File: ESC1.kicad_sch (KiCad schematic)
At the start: 35 parts, among them J7 SWD1, J8 MOTOR1, Q1 XRS306D, Q2 XRS306D, Q3 XRS306D, U8 STM32G071GBUxN, U9 DRV8300D

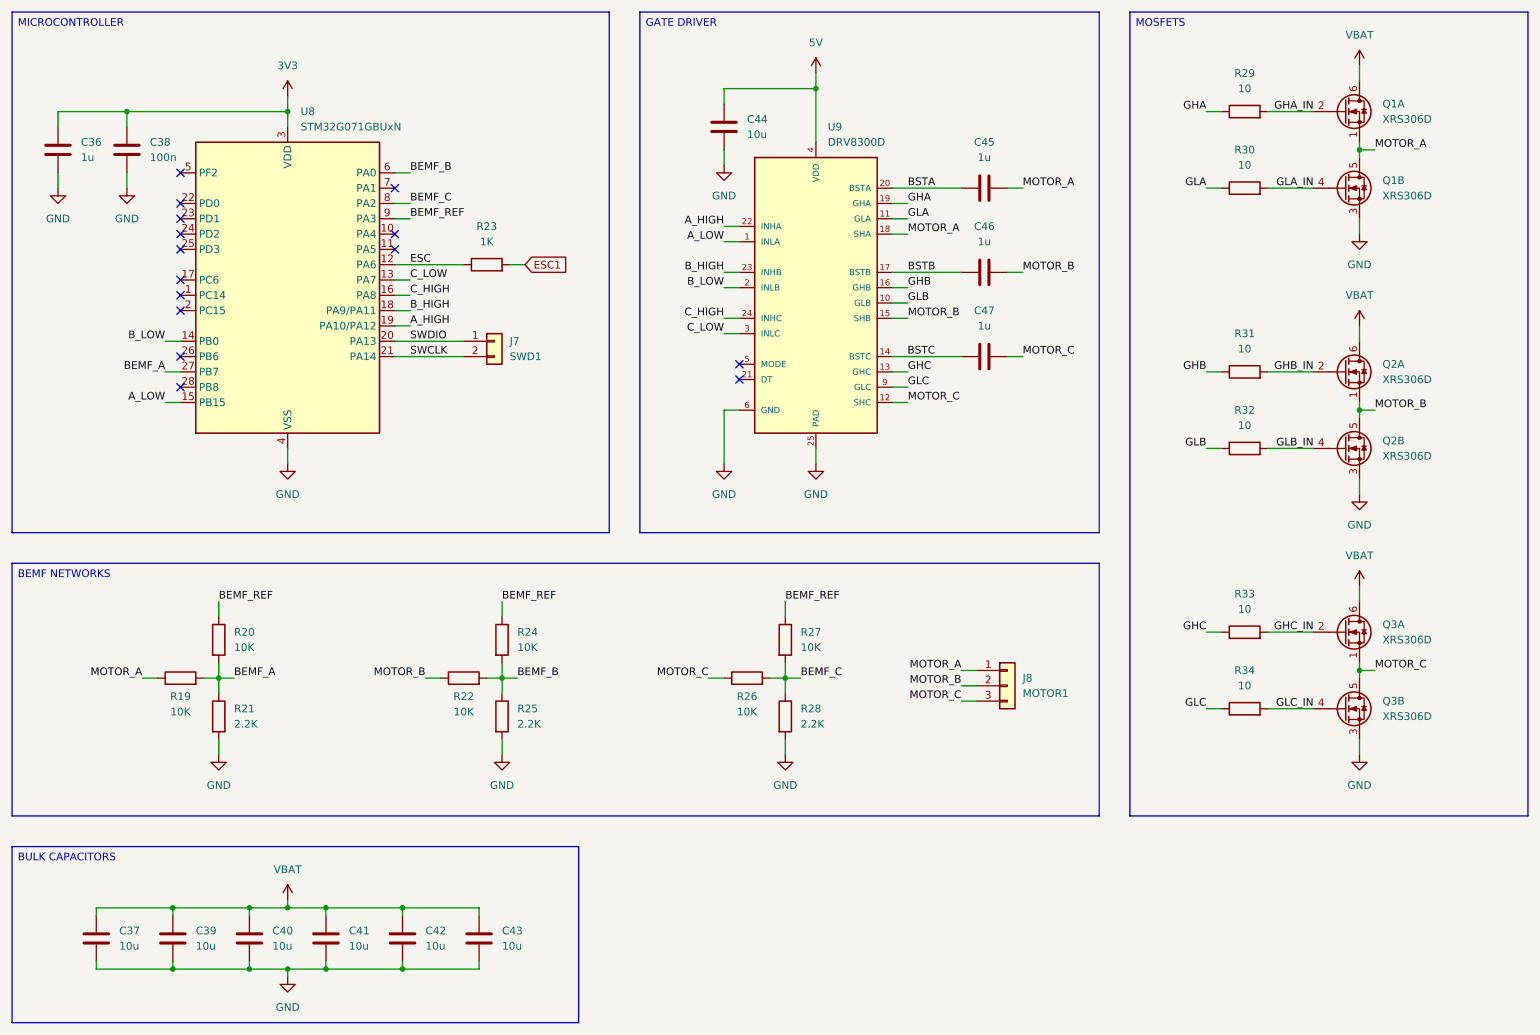
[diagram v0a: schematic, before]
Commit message: Schematic revision
Added an ESP32 C3 for the ELRS receiver.
Updated the protection approach for the board.
Updated the net nodes.
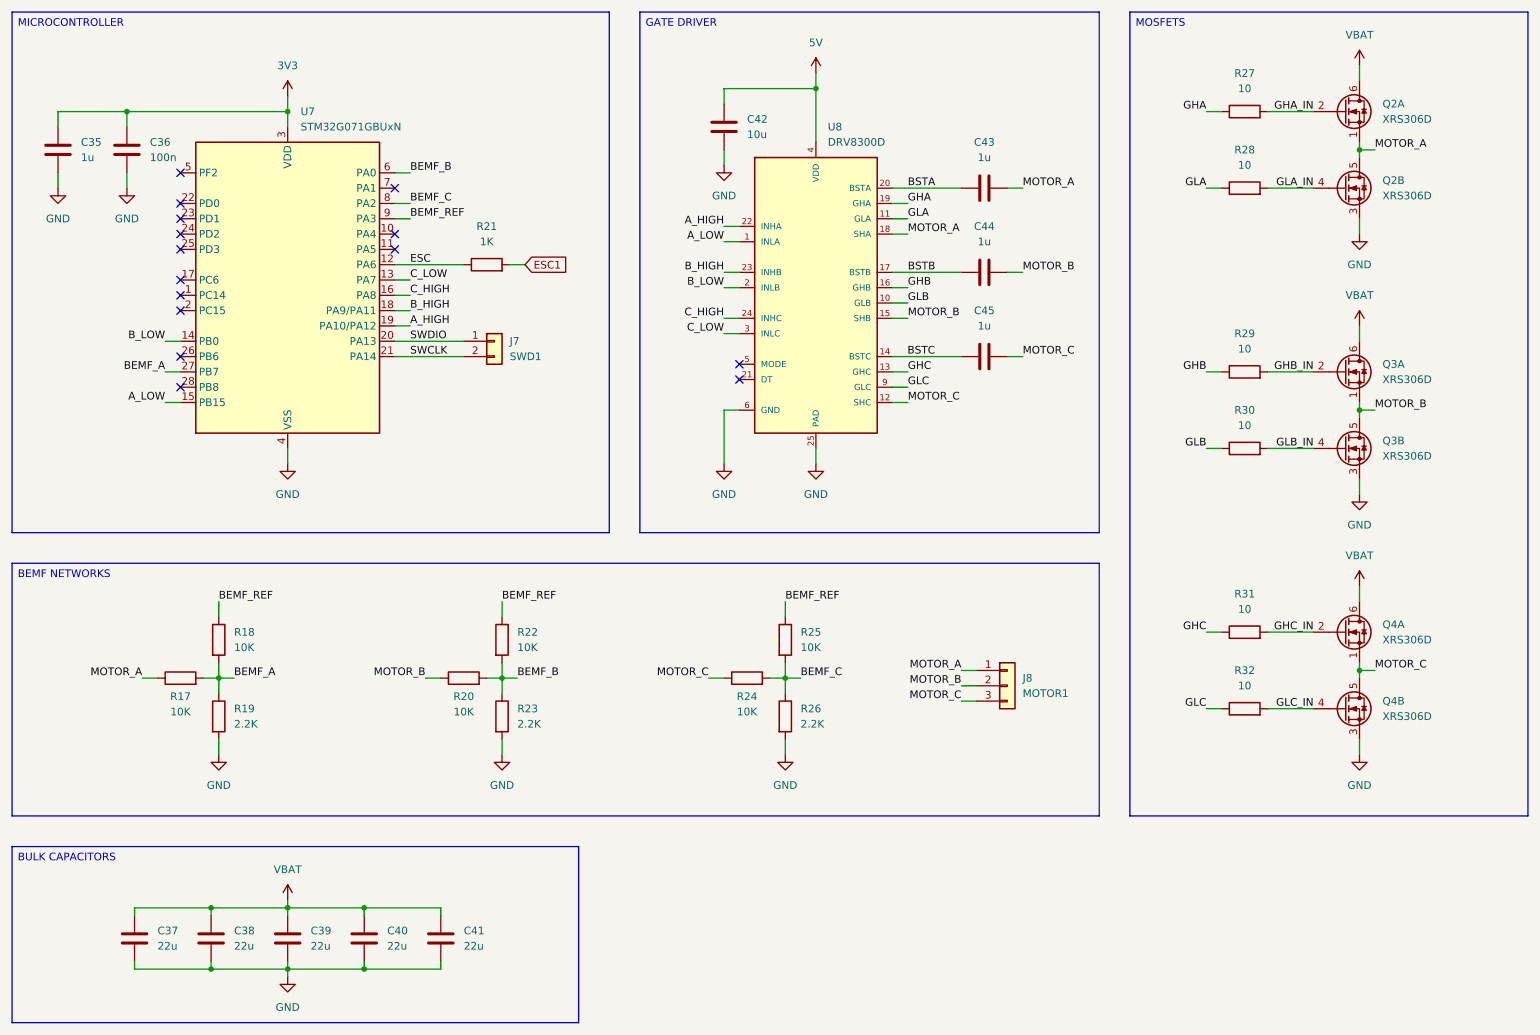
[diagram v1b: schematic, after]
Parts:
- removed C41: 10u, Capacitor_SMD:C_1206_3216Metric, symbol Device:C
- C37: value 10u -> 22u
- C38: renamed from C39; value 10u -> 22u
- C39: renamed from C40; value 10u -> 22u
- C40: renamed from C42; value 10u -> 22u
- C41: renamed from C43; value 10u -> 22u
- renumbered C36 to C35, C38 to C36, C44 to C42, C45 to C43, C46 to C44, C47 to C45, Q1 to Q2, Q2 to Q3, Q3 to Q4, R19 to R17, R20 to R18, R21 to R19, R22 to R20, R23 to R21, R24 to R22, R25 to R23, R26 to R24, R27 to R25, R28 to R26, R29 to R27, R30 to R28, R31 to R29, R32 to R30, R33 to R31, R34 to R32, U8 to U7, U9 to U8
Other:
- moved on the sheet: C37, C38, C39, C40, C41

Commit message: IMU filtering and layout
Added a missing capacitor for the IMU.
Updated the PCB layout.
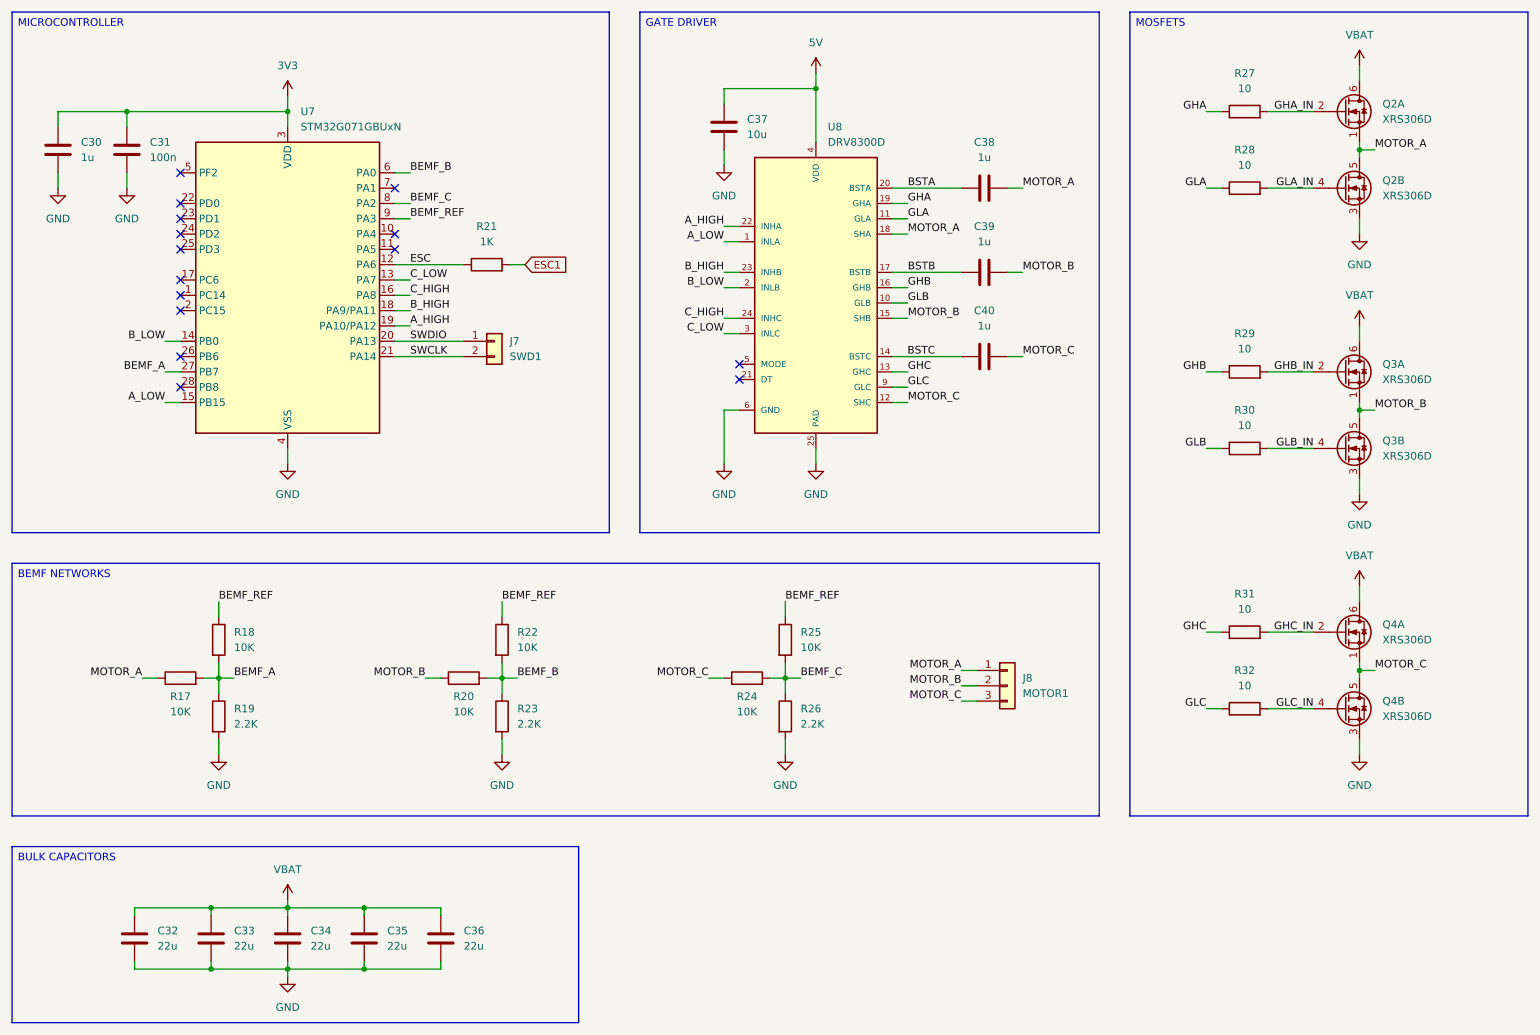
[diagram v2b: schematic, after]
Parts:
- renumbered C35 to C30, C36 to C31, C37 to C32, C38 to C33, C39 to C34, C40 to C35, C41 to C36, C42 to C37, C43 to C38, C44 to C39, C45 to C40

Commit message: Oscillator and IMU layout
Updated the oscillator layout for the RP2350.
Updated the IMU layout for the IMU.
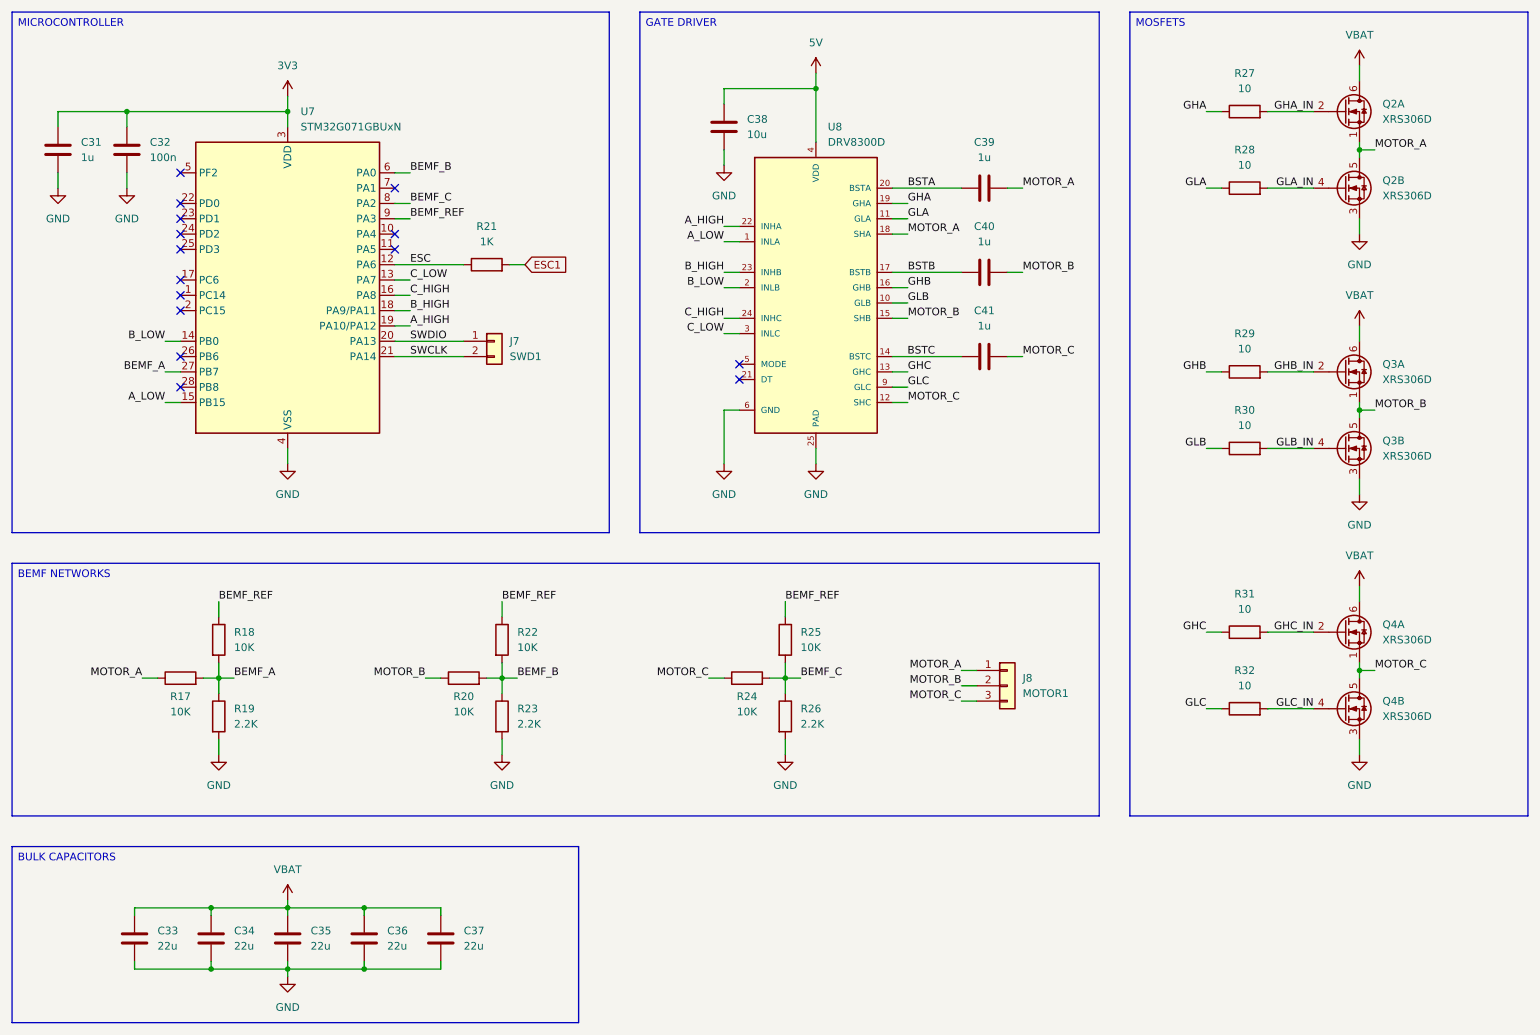
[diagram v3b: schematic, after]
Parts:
- renumbered C30 to C31, C31 to C32, C32 to C33, C33 to C34, C34 to C35, C35 to C36, C36 to C37, C37 to C38, C38 to C39, C39 to C40, C40 to C41
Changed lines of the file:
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@@
 		(dnp no)
 		(fields_autoplaced yes)
-		(property "Reference" "C39"
+		(property "Reference" "C40"
 			(at 184.15 58.42 90)
 			(effects
@@
 			(project "ThunderHorse"
 				(path "/ac187c6c-fa53-41cc-bce1-6f39a42a92e8/807a5f6f-4255-4cf0-8d90-acd62bb18590/1e531f33-ba68-434b-8668-a85d28098a3f"
-					(reference "C39")
+					(reference "C40")
 					(unit 1)
 				)
@@
 		(dnp no)
 		(fields_autoplaced yes)
-		(property "Reference" "C33"
+		(property "Reference" "C34"
 			(at 59.69 175.2599 0)
 			(effects
@@
 			(project "ThunderHorse"
 				(path "/ac187c6c-fa53-41cc-bce1-6f39a42a92e8/807a5f6f-4255-4cf0-8d90-acd62bb18590/1e531f33-ba68-434b-8668-a85d28098a3f"
-					(reference "C33")
+					(reference "C34")
 					(unit 1)
 				)
@@
 		(dnp no)
 		(fields_autoplaced yes)
-		(property "Reference" "C37"
+		(property "Reference" "C38"
 			(at 144.78 40.6399 0)
 			(effects
@@
 			(project "ThunderHorse"
 				(path "/ac187c6c-fa53-41cc-bce1-6f39a42a92e8/807a5f6f-4255-4cf0-8d90-acd62bb18590/1e531f33-ba68-434b-8668-a85d28098a3f"
-					(reference "C37")
+					(reference "C38")
 					(unit 1)
 				)
@@
 		(dnp no)
 		(fields_autoplaced yes)
-		(property "Reference" "C40"
+		(property "Reference" "C41"
 			(at 184.15 72.39 90)
 			(effects
@@
 			(project "ThunderHorse"
 				(path "/ac187c6c-fa53-41cc-bce1-6f39a42a92e8/807a5f6f-4255-4cf0-8d90-acd62bb18590/1e531f33-ba68-434b-8668-a85d28098a3f"
-					(reference "C40")
+					(reference "C41")
 					(unit 1)
 				)
@@
 		(dnp no)
 		(fields_autoplaced yes)
-		(property "Reference" "C35"
+		(property "Reference" "C36"
 			(at 85.09 175.2599 0)
 			(effects
@@
 			(project "ThunderHorse"
 				(path "/ac187c6c-fa53-41cc-bce1-6f39a42a92e8/807a5f6f-4255-4cf0-8d90-acd62bb18590/1e531f33-ba68-434b-8668-a85d28098a3f"
-					(reference "C35")
+					(reference "C36")
 					(unit 1)
 				)
@@
 		(dnp no)
 		(fields_autoplaced yes)
-		(property "Reference" "C31"
+		(property "Reference" "C32"
 			(at 45.72 44.4499 0)
 			(effects
@@
 			(project "ThunderHorse"
 				(path "/ac187c6c-fa53-41cc-bce1-6f39a42a92e8/807a5f6f-4255-4cf0-8d90-acd62bb18590/1e531f33-ba68-434b-8668-a85d28098a3f"
-					(reference "C31")
+					(reference "C32")
 					(unit 1)
 				)
@@
 		(dnp no)
 		(fields_autoplaced yes)
-		(property "Reference" "C34"
+		(property "Reference" "C35"
 			(at 72.39 175.2599 0)
 			(effects
@@
 			(project "ThunderHorse"
 				(path "/ac187c6c-fa53-41cc-bce1-6f39a42a92e8/807a5f6f-4255-4cf0-8d90-acd62bb18590/1e531f33-ba68-434b-8668-a85d28098a3f"
-					(reference "C34")
+					(reference "C35")
 					(unit 1)
 				)
@@
 		(on_board yes)
 		(dnp no)
-		(property "Reference" "C32"
+		(property "Reference" "C33"
 			(at 46.99 175.2599 0)
 			(effects
@@
 			(project ""
 				(path "/ac187c6c-fa53-41cc-bce1-6f39a42a92e8/807a5f6f-4255-4cf0-8d90-acd62bb18590/1e531f33-ba68-434b-8668-a85d28098a3f"
-					(reference "C32")
+					(reference "C33")
 					(unit 1)
 				)
@@
 		(dnp no)
 		(fields_autoplaced yes)
-		(property "Reference" "C30"
+		(property "Reference" "C31"
 			(at 34.29 44.4499 0)
 			(effects
@@
 			(project "ThunderHorse"
 				(path "/ac187c6c-fa53-41cc-bce1-6f39a42a92e8/807a5f6f-4255-4cf0-8d90-acd62bb18590/1e531f33-ba68-434b-8668-a85d28098a3f"
-					(reference "C30")
+					(reference "C31")
 					(unit 1)
 				)
@@
 		(dnp no)
 		(fields_autoplaced yes)
-		(property "Reference" "C38"
+		(property "Reference" "C39"
 			(at 184.15 44.45 90)
 			(effects
@@
 			(project "ThunderHorse"
 				(path "/ac187c6c-fa53-41cc-bce1-6f39a42a92e8/807a5f6f-4255-4cf0-8d90-acd62bb18590/1e531f33-ba68-434b-8668-a85d28098a3f"
-					(reference "C38")
+					(reference "C39")
 					(unit 1)
 				)
@@
 		(dnp no)
 		(fields_autoplaced yes)
-		(property "Reference" "C36"
+		(property "Reference" "C37"
 			(at 97.79 175.2599 0)
 			(effects
@@
 			(project "ThunderHorse"
 				(path "/ac187c6c-fa53-41cc-bce1-6f39a42a92e8/807a5f6f-4255-4cf0-8d90-acd62bb18590/1e531f33-ba68-434b-8668-a85d28098a3f"
-					(reference "C36")
+					(reference "C37")
 					(unit 1)
 				)

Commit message: Power and ESC layout
Updated the power layout.
Updated the ESC layout.

TODO:
Improve track spacing for the ESC.
Complete the power connections.
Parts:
- C38: footprint Capacitor_SMD:C_0805_2012Metric -> Capacitor_SMD:C_0603_1608Metric
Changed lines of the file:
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@@
 			)
 		)
-		(property "Footprint" "Capacitor_SMD:C_0805_2012Metric"
+		(property "Footprint" "Capacitor_SMD:C_0603_1608Metric"
 			(at 141.9352 45.72 0)
 			(effects
